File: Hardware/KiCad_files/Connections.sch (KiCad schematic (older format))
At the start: 6 parts

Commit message: Upgraded FPGA
Changed FPGA part from XC7A25T to XC7A35T
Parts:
- removed U? (x3): XC7A25T_CSG325, symbol XC7A25T_CSG325
- added U? (x3): XC7A35T_CSG325, symbol XC7A35T_CSG325
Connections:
- net D00: now also U?.K16 (IO_L1P_T0_D00_MOSI_14)
- net D01: now also U?.L17 (IO_L1N_T0_D01_DIN_14)
- net D02: now also U?.J15 (IO_L2P_T0_D02_14)
- net D03: now also U?.J16 (IO_L2N_T0_D03_14)
- net EMCCLK: now also U?.K18 (IO_L3N_T0_DQS_EMCCLK_14)
- net FCS_B: now also U?.L15 (IO_L6P_T0_FCS_B_14)
- net HDMI_INT: now also U?.U12 (IO_L22N_T3_A04_D20_14)
- net HDMI_R_CLK: now also U?.T12 (IO_L22P_T3_A05_D21_14)
- net HDMI_R_D10: now also U?.T17 (IO_L16P_T2_CSI_B_14)
- net HDMI_R_D11: now also U?.P15 (IO_L11P_T1_SRCC_14)
- net HDMI_R_D16: now also U?.P18 (IO_L10N_T1_D15_14)
- net HDMI_R_D17: now also U?.T18 (IO_L15N_T2_DQS_DOUT_CSO_B_14)
- net HDMI_R_D18: now also U?.U9 (IO_L24P_T3_A01_D17_14)
- net HDMI_R_D19: now also U?.U14 (IO_L20P_T3_A08_D24_14)
- net HDMI_R_D20: now also U?.V9 (IO_L24N_T3_A00_D16_14)
- net HDMI_R_D21: now also U?.N18 (IO_L10P_T1_D14_14)
- net HDMI_R_D22: now also U?.U10 (IO_25_14)
- net HDMI_R_D23: now also U?.T13 (IO_L19N_T3_A09_D25_VREF_14)
- net HDMI_R_D28: now also U?.V16 (IO_L18P_T2_A12_D28_14)
- net HDMI_R_D29: now also U?.R18 (IO_L15P_T2_DQS_RDWR_B_14)
- net HDMI_R_D30: now also U?.U15 (IO_L17P_T2_A14_D30_14)
- net HDMI_R_D31: now also U?.R13 (IO_L19P_T3_A10_D26_14)
- net HDMI_R_D32: now also U?.V17 (IO_L18N_T2_A11_D27_14)
- net HDMI_R_D33: now also U?.V14 (IO_L20N_T3_A07_D23_14)
- net HDMI_R_D34: now also U?.V12 (IO_L21P_T3_DQS_14)
- net HDMI_R_D35: now also U?.V13 (IO_L21N_T3_DQS_A06_D22_14)
- net HDMI_R_D4: now also U?.U17 (IO_L16N_T2_A15_D31_14)
- net HDMI_R_D5: now also U?.R17 (IO_L14N_T2_SRCC_14)
- net HDMI_R_D6: now also U?.R16 (IO_L14P_T2_SRCC_14)
- net HDMI_R_D7: now also U?.P16 (IO_L11N_T1_SRCC_14)
- net HDMI_R_D8: now also U?.P14 (IO_L12P_T1_MRCC_14)
- net HDMI_R_D9: now also U?.T15 (IO_L13N_T2_MRCC_14)
- net HDMI_R_DE: now also U?.R15 (IO_L12N_T1_MRCC_14)
- net HDMI_R_HSYNC: now also U?.U16 (IO_L17N_T2_A13_D29_14)
- net HDMI_R_SPDIF: now also U?.U11 (IO_L23P_T3_A03_D19_14)
- net HDMI_R_VSYNC: now also U?.T14 (IO_L13P_T2_MRCC_14)
- net HDMI_SPDIF_OUT_LS: now also U?.V11 (IO_L23N_T3_A02_D18_14)
- net PCIe_PERST: now also U?.M14 (IO_L8P_T1_D11_14)
- net PCIe_WAKE_B: now also U?.M17 (IO_L7N_T1_D10_14)
- net TTL_CTS1: now also U?.K15 (IO_L5N_T0_D07_14)
- net TTL_DCD1: now also U?.N16 (IO_L9P_T1_DQS_14)
- net TTL_DSR1: now also U?.N14 (IO_L8N_T1_D12_14)
- net TTL_DTR1: now also U?.M16 (IO_L7P_T1_D09_14)
- net TTL_RI1: now also U?.N17 (IO_L9N_T1_DQS_D13_14)
- net TTL_RTS1: now also U?.J14 (IO_L5P_T0_D06_14)
- net TTL_RxD1: now also U?.L18 (IO_L4N_T0_D05_14)
- net TTL_TxD1: now also U?.K17 (IO_L4P_T0_D04_14)
- net VCCO: now also U?.A16 (VCCO_15), U?.B13 (VCCO_15), U?.C10 (VCCO_15), U?.D17 (VCCO_15), U?.E14 (VCCO_15), U?.G18 (VCCO_15), U?.H15 (VCCO_15), U?.J18 (IO_L3P_T0_DQS_PUDC_B_14), U?.L16 (VCCO_14), U?.L6 (VCCO_34), U?.M3 (VCCO_34), U?.P17 (VCCO_14), U?.P7 (VCCO_34), U?.R14 (VCCO_14), U?.R4 (VCCO_34), U?.T1 (VCCO_34), U?.T11 (VCCO_14), U?.U18 (VCCO_14), U?.U8 (VCCO_14), U?.V15 (VCCO_14), U?.V5 (VCCO_34)
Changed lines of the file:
@@
 LIBS:valves
 LIBS:custom
-LIBS:pcie_test_1-cache
+LIBS:RASAC-cache
 EELAYER 25 0
 EELAYER END
@@
 Comment4 "The Cooper Union for the Advancement of Science and Art"
 $EndDescr
-$Comp
-L XC7A25T_CSG325 U?
-U 2 1 5C11344D
-P 2150 6300
-AR Path="/5C064F83/5C11344D" Ref="U?"  Part="2"
-AR Path="/5C0630AC/5C11344D" Ref="U?"  Part="2"
-F 0 "U?" H 2150 6000 60  0000 C CNN
-F 1 "XC7A25T_CSG325" H 2150 6100 60  0000 C CNN
-F 2 "" H 2450 8050 60  0001 C CNN
-F 3 "" H 2450 8050 60  0001 C CNN
-	2    2150 6300
-	1    0    0    -1
-$EndComp
 Text GLabel 950  5700 0    60   Input ~ 0
 VCCO
@@
 Text GLabel 3150 1900 2    60   Input ~ 0
 VCCO
-$Comp
-L XC7A25T_CSG325 U?
-U 3 1 5C13C290
-P 5400 6300
-AR Path="/5C064F83/5C13C290" Ref="U?"  Part="3"
-AR Path="/5C0652F6/5C13C290" Ref="U?"  Part="3"
-F 0 "U?" H 5400 6000 60  0000 C CNN
-F 1 "XC7A25T_CSG325" H 5400 6100 60  0000 C CNN
-F 2 "" H 5700 8050 60  0001 C CNN
-F 3 "" H 5700 8050 60  0001 C CNN
-	3    5400 6300
-	1    0    0    -1
-$EndComp
-$Comp
-L XC7A25T_CSG325 U?
-U 4 1 5C13C297
-P 8300 5850
-AR Path="/5C064F83/5C13C297" Ref="U?"  Part="4"
-AR Path="/5C0652F6/5C13C297" Ref="U?"  Part="4"
-F 0 "U?" H 8300 5550 60  0000 C CNN
-F 1 "XC7A25T_CSG325" H 8300 5650 60  0000 C CNN
-F 2 "" H 8600 7600 60  0001 C CNN
-F 3 "" H 8600 7600 60  0001 C CNN
-	4    8300 5850
-	1    0    0    -1
-$EndComp
 Text GLabel 4300 5700 0    60   Input ~ 0
 VCCO
@@
 Text GLabel 3150 3200 2    60   Input ~ 0
 TTL_RI1
+$Comp
+L XC7A35T_CSG325 U?
+U 2 1 5C174C53
+P 2150 6300
+F 0 "U?" H 2150 6000 60  0000 C CNN
+F 1 "XC7A35T_CSG325" H 2150 6100 60  0000 C CNN
+F 2 "" H 2450 8050 60  0001 C CNN
+F 3 "" H 2450 8050 60  0001 C CNN
+	2    2150 6300
+	1    0    0    -1
+$EndComp
+$Comp
+L XC7A35T_CSG325 U?
+U 3 1 5C174C9A
+P 5400 6300
+F 0 "U?" H 5400 6000 60  0000 C CNN
+F 1 "XC7A35T_CSG325" H 5400 6100 60  0000 C CNN
+F 2 "" H 5700 8050 60  0001 C CNN
+F 3 "" H 5700 8050 60  0001 C CNN
+	3    5400 6300
+	1    0    0    -1
+$EndComp
+$Comp
+L XC7A35T_CSG325 U?
+U 4 1 5C174CD5
+P 8300 5850
+F 0 "U?" H 8300 5550 60  0000 C CNN
+F 1 "XC7A35T_CSG325" H 8300 5650 60  0000 C CNN
+F 2 "" H 8600 7600 60  0001 C CNN
+F 3 "" H 8600 7600 60  0001 C CNN
+	4    8300 5850
+	1    0    0    -1
+$EndComp
 $EndSCHEMATC

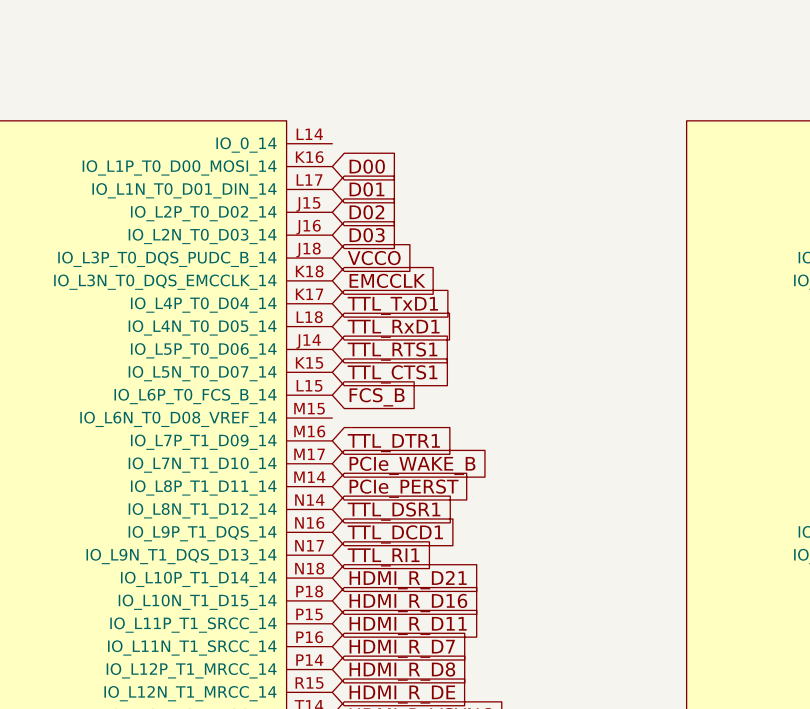
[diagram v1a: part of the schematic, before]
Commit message: Added SYSCLK
Changed EMCCLK from SiT8103 to SiT8209 because Digikey didn't have.
Added SiT9102 200MHz for SYSCLK
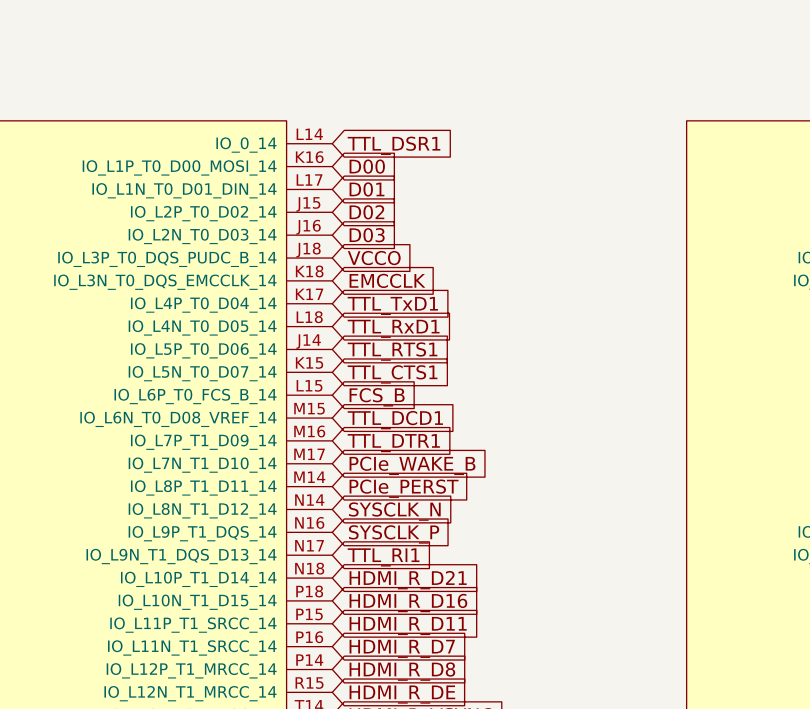
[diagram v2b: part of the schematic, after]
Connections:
- net TTL_DCD1: now also U?.M15 (IO_L6N_T0_D08_VREF_14); no longer U?.N16 (IO_L9P_T1_DQS_14)
- net TTL_DSR1: now also U?.L14 (IO_0_14); no longer U?.N14 (IO_L8N_T1_D12_14)
- new net SYSCLK_N: U?.N14 (IO_L8N_T1_D12_14)
- new net SYSCLK_P: U?.N16 (IO_L9P_T1_DQS_14)
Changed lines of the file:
@@
 Text GLabel 3150 2700 2    60   Input ~ 0
 TTL_DTR1
-Text GLabel 3150 3000 2    60   Input ~ 0
+Text GLabel 3150 1400 2    60   Input ~ 0
 TTL_DSR1
-Text GLabel 3150 3100 2    60   Input ~ 0
+Text GLabel 3150 2600 2    60   Input ~ 0
 TTL_DCD1
 Text GLabel 3150 3200 2    60   Input ~ 0
@@
 	1    0    0    -1
 $EndComp
+Text GLabel 3150 3000 2    60   Input ~ 0
+SYSCLK_N
+Text GLabel 3150 3100 2    60   Input ~ 0
+SYSCLK_P
 $EndSCHEMATC

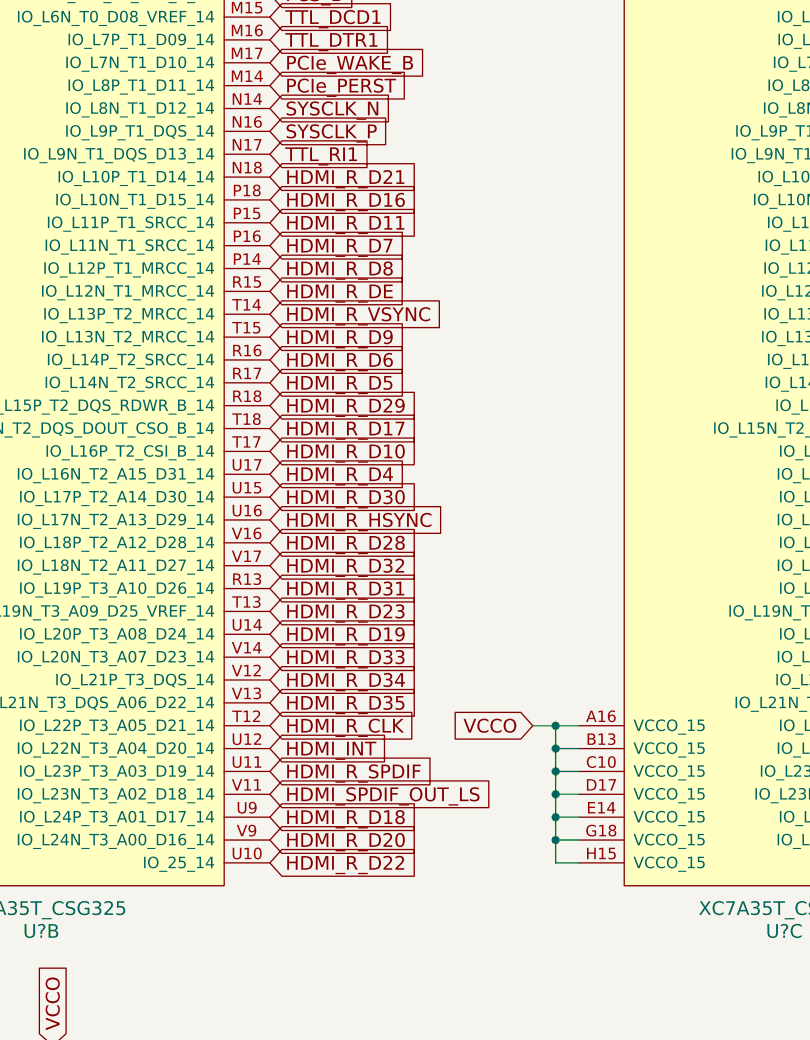
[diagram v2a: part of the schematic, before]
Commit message: Added  HDMI transmitter chip
Also added resistors and moved HDMI data pins around on FPGA side
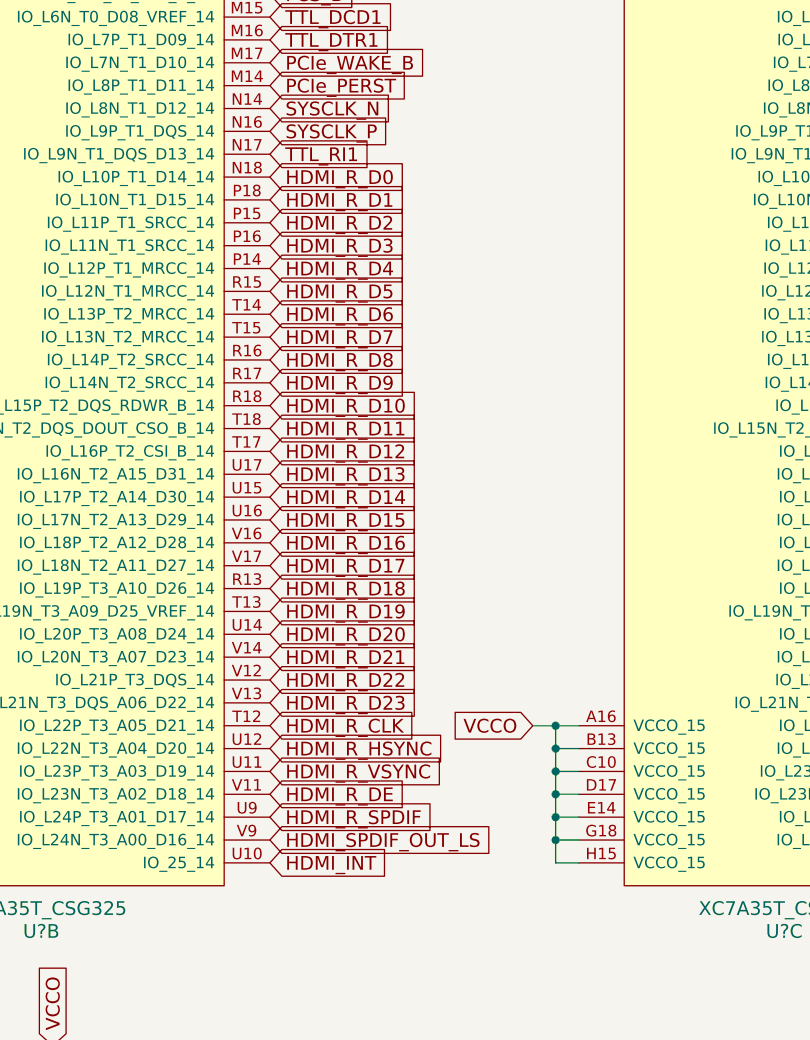
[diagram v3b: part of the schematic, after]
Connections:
- net HDMI_R_D28 is gone; now on net HDMI_R_D16: U?.V16 (IO_L18P_T2_A12_D28_14)
- net HDMI_R_D29 is gone; now on net HDMI_R_D10: U?.R18 (IO_L15P_T2_DQS_RDWR_B_14)
- net HDMI_R_D31 is gone; now on net HDMI_R_D18: U?.R13 (IO_L19P_T3_A10_D26_14)
- net HDMI_R_D32 is gone; now on net HDMI_R_D17: U?.V17 (IO_L18N_T2_A11_D27_14)
- net HDMI_R_D33 is gone; now on net HDMI_R_D21: U?.V14 (IO_L20N_T3_A07_D23_14)
- net HDMI_R_D34 is gone; now on net HDMI_R_D22: U?.V12 (IO_L21P_T3_DQS_14)
- net HDMI_R_D35 is gone; now on net HDMI_R_D23: U?.V13 (IO_L21N_T3_DQS_A06_D22_14)
- net HDMI_INT: now also U?.U10 (IO_25_14); no longer U?.U12 (IO_L22N_T3_A04_D20_14)
- net HDMI_R_D10: no longer U?.T17 (IO_L16P_T2_CSI_B_14)
- net HDMI_R_D11: now also U?.T18 (IO_L15N_T2_DQS_DOUT_CSO_B_14); no longer U?.P15 (IO_L11P_T1_SRCC_14)
- net HDMI_R_D16: no longer U?.P18 (IO_L10N_T1_D15_14)
- net HDMI_R_D17: no longer U?.T18 (IO_L15N_T2_DQS_DOUT_CSO_B_14)
- net HDMI_R_D18: no longer U?.U9 (IO_L24P_T3_A01_D17_14)
- net HDMI_R_D19: now also U?.T13 (IO_L19N_T3_A09_D25_VREF_14); no longer U?.U14 (IO_L20P_T3_A08_D24_14)
- net HDMI_R_D20: now also U?.U14 (IO_L20P_T3_A08_D24_14); no longer U?.V9 (IO_L24N_T3_A00_D16_14)
- net HDMI_R_D21: no longer U?.N18 (IO_L10P_T1_D14_14)
- net HDMI_R_D22: no longer U?.U10 (IO_25_14)
- net HDMI_R_D23: no longer U?.T13 (IO_L19N_T3_A09_D25_VREF_14)
- net HDMI_R_D4: now also U?.P14 (IO_L12P_T1_MRCC_14); no longer U?.U17 (IO_L16N_T2_A15_D31_14)
- net HDMI_R_D5: now also U?.R15 (IO_L12N_T1_MRCC_14); no longer U?.R17 (IO_L14N_T2_SRCC_14)
- net HDMI_R_D6: now also U?.T14 (IO_L13P_T2_MRCC_14); no longer U?.R16 (IO_L14P_T2_SRCC_14)
- net HDMI_R_D7: now also U?.T15 (IO_L13N_T2_MRCC_14); no longer U?.P16 (IO_L11N_T1_SRCC_14)
- net HDMI_R_D8: now also U?.R16 (IO_L14P_T2_SRCC_14); no longer U?.P14 (IO_L12P_T1_MRCC_14)
- net HDMI_R_D9: now also U?.R17 (IO_L14N_T2_SRCC_14); no longer U?.T15 (IO_L13N_T2_MRCC_14)
- net HDMI_R_DE: now also U?.V11 (IO_L23N_T3_A02_D18_14); no longer U?.R15 (IO_L12N_T1_MRCC_14)
- net HDMI_R_HSYNC: now also U?.U12 (IO_L22N_T3_A04_D20_14); no longer U?.U16 (IO_L17N_T2_A13_D29_14)
- net HDMI_R_SPDIF: now also U?.U9 (IO_L24P_T3_A01_D17_14); no longer U?.U11 (IO_L23P_T3_A03_D19_14)
- net HDMI_R_VSYNC: now also U?.U11 (IO_L23P_T3_A03_D19_14); no longer U?.T14 (IO_L13P_T2_MRCC_14)
- net HDMI_SPDIF_OUT_LS: now also U?.V9 (IO_L24N_T3_A00_D16_14); no longer U?.V11 (IO_L23N_T3_A02_D18_14)
- net HDMI_R_D30 renamed HDMI_R_D14
- new net HDMI_R_D0: U?.N18 (IO_L10P_T1_D14_14)
- new net HDMI_R_D1: U?.P18 (IO_L10N_T1_D15_14)
- new net HDMI_R_D12: U?.T17 (IO_L16P_T2_CSI_B_14)
- new net HDMI_R_D13: U?.U17 (IO_L16N_T2_A15_D31_14)
- new net HDMI_R_D15: U?.U16 (IO_L17N_T2_A13_D29_14)
- new net HDMI_R_D2: U?.P15 (IO_L11P_T1_SRCC_14)
- new net HDMI_R_D3: U?.P16 (IO_L11N_T1_SRCC_14)
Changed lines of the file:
@@
 Connection ~ 7500 5450
 Text GLabel 3150 3300 2    60   Input ~ 0
+HDMI_R_D0
+Text GLabel 3150 3400 2    60   Input ~ 0
+HDMI_R_D1
+Text GLabel 3150 3500 2    60   Input ~ 0
+HDMI_R_D2
+Text GLabel 3150 3600 2    60   Input ~ 0
+HDMI_R_D3
+Text GLabel 3150 3700 2    60   Input ~ 0
+HDMI_R_D4
+Text GLabel 3150 3800 2    60   Input ~ 0
+HDMI_R_D5
+Text GLabel 3150 3900 2    60   Input ~ 0
+HDMI_R_D6
+Text GLabel 3150 4000 2    60   Input ~ 0
+HDMI_R_D7
+Text GLabel 3150 4100 2    60   Input ~ 0
+HDMI_R_D8
+Text GLabel 3150 4200 2    60   Input ~ 0
+HDMI_R_D9
+Text GLabel 3150 4300 2    60   Input ~ 0
+HDMI_R_D10
+Text GLabel 3150 4400 2    60   Input ~ 0
+HDMI_R_D11
+Text GLabel 3150 4500 2    60   Input ~ 0
+HDMI_R_D12
+Text GLabel 3150 4600 2    60   Input ~ 0
+HDMI_R_D13
+Text GLabel 3150 4700 2    60   Input ~ 0
+HDMI_R_D14
+Text GLabel 3150 4800 2    60   Input ~ 0
+HDMI_R_D15
+Text GLabel 3150 4900 2    60   Input ~ 0
+HDMI_R_D16
+Text GLabel 3150 5000 2    60   Input ~ 0
+HDMI_R_D17
+Text GLabel 3150 5100 2    60   Input ~ 0
+HDMI_R_D18
+Text GLabel 3150 5200 2    60   Input ~ 0
+HDMI_R_D19
+Text GLabel 3150 5300 2    60   Input ~ 0
+HDMI_R_D20
+Text GLabel 3150 5400 2    60   Input ~ 0
 HDMI_R_D21
-Text GLabel 3150 3400 2    60   Input ~ 0
-HDMI_R_D16
-Text GLabel 3150 3500 2    60   Input ~ 0
-HDMI_R_D11
-Text GLabel 3150 3600 2    60   Input ~ 0
-HDMI_R_D7
-Text GLabel 3150 3700 2    60   Input ~ 0
-HDMI_R_D8
-Text GLabel 3150 3800 2    60   Input ~ 0
-HDMI_R_DE
-Text GLabel 3150 3900 2    60   Input ~ 0
-HDMI_R_VSYNC
-Text GLabel 3150 4000 2    60   Input ~ 0
-HDMI_R_D9
-Text GLabel 3150 4100 2    60   Input ~ 0
-HDMI_R_D6
-Text GLabel 3150 4200 2    60   Input ~ 0
-HDMI_R_D5
-Text GLabel 3150 4300 2    60   Input ~ 0
-HDMI_R_D29
-Text GLabel 3150 4400 2    60   Input ~ 0
-HDMI_R_D17
-Text GLabel 3150 4500 2    60   Input ~ 0
-HDMI_R_D10
-Text GLabel 3150 4600 2    60   Input ~ 0
-HDMI_R_D4
-Text GLabel 3150 4700 2    60   Input ~ 0
-HDMI_R_D30
-Text GLabel 3150 4800 2    60   Input ~ 0
-HDMI_R_HSYNC
-Text GLabel 3150 4900 2    60   Input ~ 0
-HDMI_R_D28
-Text GLabel 3150 5000 2    60   Input ~ 0
-HDMI_R_D32
-Text GLabel 3150 5100 2    60   Input ~ 0
-HDMI_R_D31
-Text GLabel 3150 5200 2    60   Input ~ 0
+Text GLabel 3150 5500 2    60   Input ~ 0
+HDMI_R_D22
+Text GLabel 3150 5600 2    60   Input ~ 0
 HDMI_R_D23
-Text GLabel 3150 5300 2    60   Input ~ 0
-HDMI_R_D19
-Text GLabel 3150 5400 2    60   Input ~ 0
-HDMI_R_D33
-Text GLabel 3150 5500 2    60   Input ~ 0
-HDMI_R_D34
-Text GLabel 3150 5600 2    60   Input ~ 0
-HDMI_R_D35
 Text GLabel 3150 5700 2    60   Input ~ 0
 HDMI_R_CLK
+Text GLabel 3150 6300 2    60   Input ~ 0
+HDMI_INT
+Text GLabel 3150 6100 2    60   Input ~ 0
+HDMI_R_SPDIF
+Text GLabel 3150 6200 2    60   Input ~ 0
+HDMI_SPDIF_OUT_LS
 Text GLabel 3150 5800 2    60   Input ~ 0
-HDMI_INT
+HDMI_R_HSYNC
 Text GLabel 3150 5900 2    60   Input ~ 0
-HDMI_R_SPDIF
+HDMI_R_VSYNC
 Text GLabel 3150 6000 2    60   Input ~ 0
-HDMI_SPDIF_OUT_LS
-Text GLabel 3150 6100 2    60   Input ~ 0
-HDMI_R_D18
-Text GLabel 3150 6200 2    60   Input ~ 0
-HDMI_R_D20
-Text GLabel 3150 6300 2    60   Input ~ 0
-HDMI_R_D22
+HDMI_R_DE
 Text GLabel 3150 2100 2    60   Input ~ 0
 TTL_TxD1
